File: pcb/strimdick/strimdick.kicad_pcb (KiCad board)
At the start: 2 copper layers, 4 parts, among them U1 ProMicro

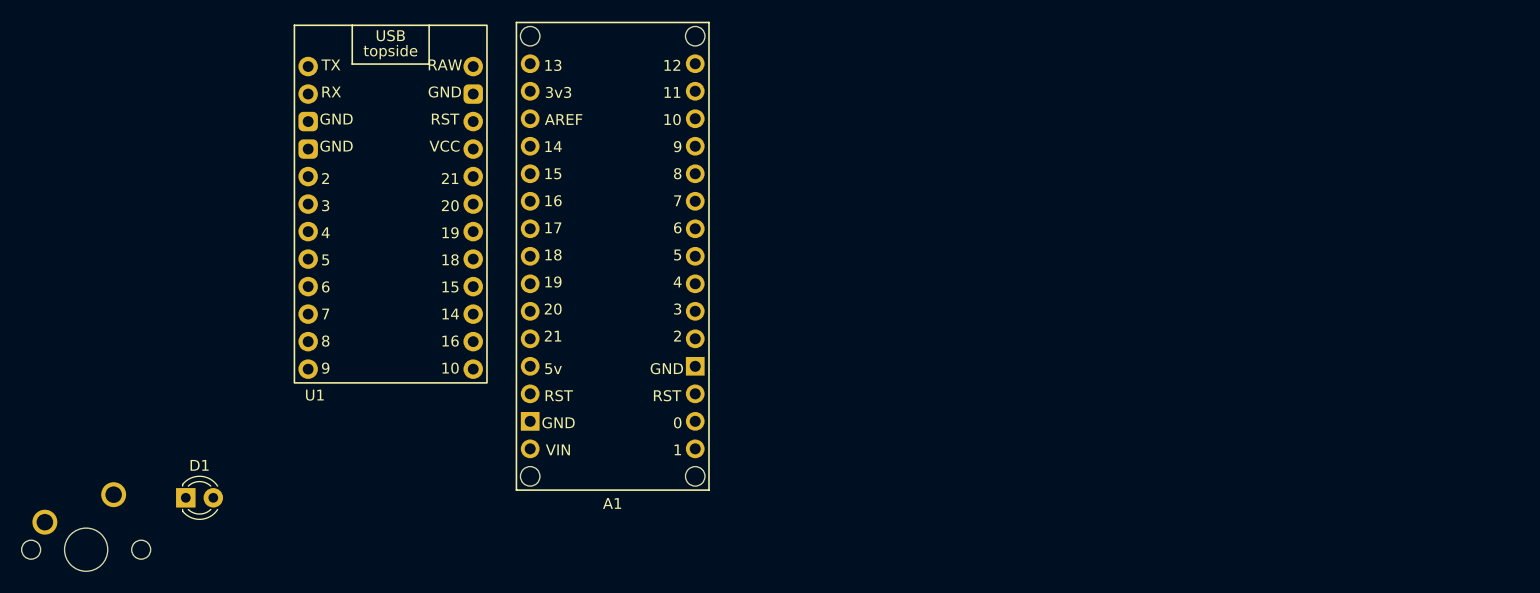
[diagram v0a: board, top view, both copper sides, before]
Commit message: Okay, got the schematic done, and a basic layout with things all stacked up, it's a bit tight
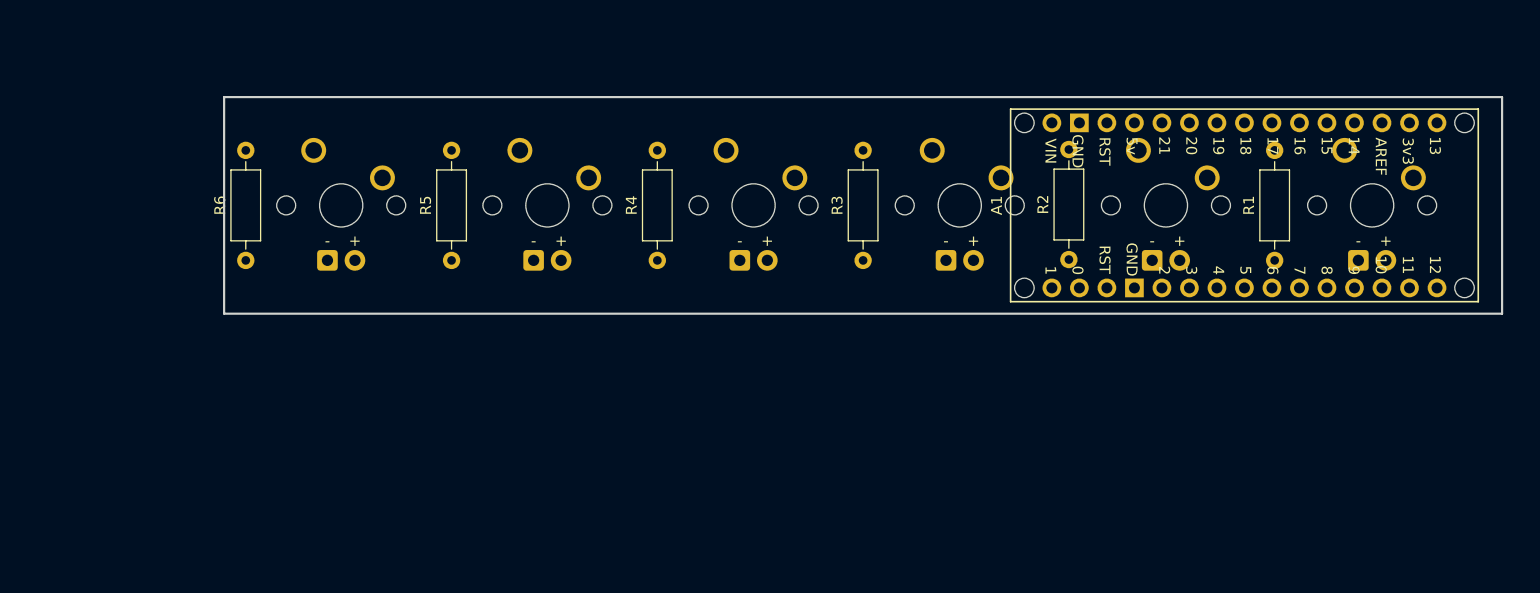
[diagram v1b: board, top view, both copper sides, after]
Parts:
- removed U1: ProMicro, Neko:ProMicro_USBup
- added D2: LED_3mm, PCM_marbastlib-mx:LED_MX_3mm, B.Cu at (156.0, 44.1)
- added D3: LED_3mm, PCM_marbastlib-mx:LED_MX_3mm, B.Cu at (136.9, 44.1)
- added D4: LED_3mm, PCM_marbastlib-mx:LED_MX_3mm, B.Cu at (117.9, 44.1)
- added D5: LED_3mm, PCM_marbastlib-mx:LED_MX_3mm, B.Cu at (98.8, 44.1)
- added D6: LED_3mm, PCM_marbastlib-mx:LED_MX_3mm, B.Cu at (79.8, 44.1)
- added MX2: MX_SW_solder, PCM_marbastlib-mx:SW_MX_1u, B.Cu at (156.0, 39.0)
- added MX3: MX_SW_solder, PCM_marbastlib-mx:SW_MX_1u, B.Cu at (136.9, 39.0)
- added MX4: MX_SW_solder, PCM_marbastlib-mx:SW_MX_1u, B.Cu at (117.9, 39.0)
- added MX5: MX_SW_solder, PCM_marbastlib-mx:SW_MX_1u, B.Cu at (98.8, 39.0)
- added MX6: MX_SW_solder, PCM_marbastlib-mx:SW_MX_1u, B.Cu at (79.8, 39.0)
- added R1: 220ohm, Resistor_THT:R_Axial_DIN0207_L6.3mm_D2.5mm_P10.16mm_Horizontal, F.Cu at (166.0, 44.1)
- added R2: 220ohm, Resistor_THT:R_Axial_DIN0207_L6.3mm_D2.5mm_P10.16mm_Horizontal, F.Cu at (147.0, 44.0)
- added R3: 220ohm, Resistor_THT:R_Axial_DIN0207_L6.3mm_D2.5mm_P10.16mm_Horizontal, F.Cu at (128.0, 44.1)
- added R4: 220ohm, Resistor_THT:R_Axial_DIN0207_L6.3mm_D2.5mm_P10.16mm_Horizontal, F.Cu at (109.0, 44.1)
- added R5: 220ohm, Resistor_THT:R_Axial_DIN0207_L6.3mm_D2.5mm_P10.16mm_Horizontal, F.Cu at (90.0, 44.1)
- added R6: 220ohm, Resistor_THT:R_Axial_DIN0207_L6.3mm_D2.5mm_P10.16mm_Horizontal, F.Cu at (71.0, 44.1)
- D1: footprint LED_THT:LED_D3.0mm -> PCM_marbastlib-mx:LED_MX_3mm; moved to B.Cu
- MX1: moved to B.Cu
- moved MX1 122.9 mm to (175.0, 39.0), turned to 180 degrees
- moved D1 111.7 mm to (175.0, 44.1), turned to 180 degrees
- moved A1 45.5 mm to (142.8, 39.0), turned to -90 degrees
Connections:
- A1 pad 5V: unconnected-(A1-Pad5V) -> Net-(A1-Pad5V)
- A1 pad A2: unconnected-(A1-PadA2) -> Net-(A1-PadA2)
- A1 pad A3: unconnected-(A1-PadA3) -> Net-(A1-PadA3)
- A1 pad A4: unconnected-(A1-A4/SDA-PadA4) -> Net-(A1-A4/SDA)
- A1 pad A5: unconnected-(A1-A5/SCL-PadA5) -> Net-(A1-A5/SCL)
- A1 pad A6: unconnected-(A1-PadA6) -> Net-(A1-PadA6)
- A1 pad A7: unconnected-(A1-PadA7) -> Net-(A1-PadA7)
- A1 pad D11: unconnected-(A1-D11_MOSI-PadD11) -> Net-(A1-D11_MOSI)
- A1 pad D2: unconnected-(A1-D2_INT0-PadD2) -> Net-(A1-D2_INT0)
- A1 pad D3: unconnected-(A1-D3_INT1-PadD3) -> Net-(A1-D3_INT1)
- A1 pad D4: unconnected-(A1-PadD4) -> Net-(A1-PadD4)
- A1 pad D5: unconnected-(A1-PadD5) -> Net-(A1-PadD5)
- A1 pad D6: unconnected-(A1-PadD6) -> Net-(A1-PadD6)
- A1 pad D7: unconnected-(A1-PadD7) -> Net-(A1-PadD7)
- A1 pad D9: unconnected-(A1-PadD9) -> Net-(A1-Pad5V)
- A1 pad GND1: unconnected-(A1-GND-PadGND1) -> Net-(A1-D11_MOSI)
- A1 pad GND2: unconnected-(A1-GND-PadGND2) -> Net-(A1-D11_MOSI)
- D1 pad 1: unconnected-(D1-Pad1) -> Net-(A1-D11_MOSI)
- D1 pad 2: unconnected-(D1-Pad2) -> Net-(D1-Pad2)
- MX1 pad 1: unconnected-(MX1-Pad1) -> Net-(A1-D11_MOSI)
- MX1 pad 2: unconnected-(MX1-Pad2) -> Net-(A1-PadA2)
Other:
- board outline added: 118 x 20 mm

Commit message: Make Design Rules Checker happy
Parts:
- moved R6 0.50 mm to (71.5, 44.1)
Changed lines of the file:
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@@
 	(footprint "Resistor_THT:R_Axial_DIN0207_L6.3mm_D2.5mm_P10.16mm_Horizontal"
 		(layer "F.Cu")
-		(at 71 44.08 90)
+		(at 71.5 44.08 90)
 		(descr "Resistor, Axial_DIN0207 series, Axial, Horizontal, pin pitch=10.16mm, 0.25W = 1/4W, length*diameter=6.3*2.5mm^2, http://cdn-reichelt.de/documents/datenblatt/B400/1_4W%23YAG.pdf")
 		(tags "Resistor Axial_DIN0207 series Axial Horizontal pin pitch 10.16mm 0.25W = 1/4W length 6.3mm diameter 2.5mm")
 		(property "Reference" "R6"
-			(at 5.08 -2.37 90)
+			(at 5.08 0 90)
 			(layer "F.SilkS")
 			(effects
@@
 		(tags "Resistor Axial_DIN0207 series Axial Horizontal pin pitch 10.16mm 0.25W = 1/4W length 6.3mm diameter 2.5mm")
 		(property "Reference" "R2"
-			(at 5.08 -2.37 90)
+			(at 5.08 0 90)
 			(layer "F.SilkS")
 			(effects
@@
 		(tags "Resistor Axial_DIN0207 series Axial Horizontal pin pitch 10.16mm 0.25W = 1/4W length 6.3mm diameter 2.5mm")
 		(property "Reference" "R4"
-			(at 5.08 -2.37 90)
+			(at 5.08 0 90)
 			(layer "F.SilkS")
 			(effects
@@
 		(tags "Resistor Axial_DIN0207 series Axial Horizontal pin pitch 10.16mm 0.25W = 1/4W length 6.3mm diameter 2.5mm")
 		(property "Reference" "R3"
-			(at 5.08 -2.37 90)
+			(at 5.08 0 90)
 			(layer "F.SilkS")
 			(effects
@@
 		(tags "Resistor Axial_DIN0207 series Axial Horizontal pin pitch 10.16mm 0.25W = 1/4W length 6.3mm diameter 2.5mm")
 		(property "Reference" "R1"
-			(at 5.08 -2.37 90)
+			(at 5.08 0 90)
 			(layer "F.SilkS")
 			(effects
@@
 		(tags "Resistor Axial_DIN0207 series Axial Horizontal pin pitch 10.16mm 0.25W = 1/4W length 6.3mm diameter 2.5mm")
 		(property "Reference" "R5"
-			(at 5.08 -2.37 90)
+			(at 5.08 0 90)
 			(layer "F.SilkS")
 			(effects
@@
 		)
 		(fp_line
-			(start 8.89 1.18)
+			(start -4 1.18)
 			(end -8.89 1.18)
 			(stroke
@@
 		(fp_line
 			(start 8.89 1.18)
+			(end 4 1.18)
+			(stroke
+				(width 0.15)
+				(type solid)
+			)
+			(layer "F.SilkS")
+		)
+		(fp_line
+			(start 8.89 1.18)
 			(end 8.89 -42)
 			(stroke
@@
 		)
 		(fp_text user "6"
-			(at 6 -23 -90)
+			(at 6 -22.1995 -90)
 			(unlocked yes)
 			(layer "F.SilkS")
@@
 		)
 		(fp_text user "14"
-			(at -5.5 -30.5 -90)
-			(unlocked yes)
-			(layer "F.SilkS")
-			(effects
-				(font
-					(size 1 1)
-					(thickness 0.15)
-				)
-			)
-		)
-		(fp_text user "9"
-			(at 6 -30.5 -90)
+			(at -5.5 -31.6995 -90)
 			(unlocked yes)
 			(layer "F.SilkS")
@@
 		)
 		(fp_text user "18"
-			(at -5.5 -20.5 -90)
-			(unlocked yes)
-			(layer "F.SilkS")
-			(effects
-				(font
-					(size 1 1)
-					(thickness 0.15)
-				)
-			)
-		)
-		(fp_text user "2"
-			(at 6 -13 -90)
+			(at -5.5 -20.1995 -90)
 			(unlocked yes)
 			(layer "F.SilkS")
@@
 			)
 		)
-		(fp_text user "10"
-			(at 5.5 -33 -90)
-			(unlocked yes)
-			(layer "F.SilkS")
-			(effects
-				(font
-					(size 1 1)
-					(thickness 0.15)
-				)
-			)
-		)
 		(fp_text user "GND"
-			(at -5 -5 -90)
+			(at -5 -5.6995 -90)
 			(unlocked yes)
 			(layer "F.SilkS")
@@
 		)
 		(fp_text user "3"
-			(at 6 -15.5 -90)
+			(at 6 -15.6995 -90)
 			(unlocked yes)
 			(layer "F.SilkS")
@@
 		)
 		(fp_text user "17"
-			(at -5.5 -23 -90)
+			(at -5.5 -21.6995 -90)
 			(unlocked yes)
 			(layer "F.SilkS")
@@
 		)
 		(fp_text user "15"
-			(at -5.5 -28 -90)
+			(at -5.5 -27.1995 -90)
 			(unlocked yes)
 			(layer "F.SilkS")
@@
 		)
 		(fp_text user "5v"
-			(at -5.5 -10 -90)
+			(at -5.5 -8.6995 -90)
 			(unlocked yes)
 			(layer "F.SilkS")
@@
 	)
 	(gr_rect
-		(start 69 29)
-		(end 187 49)
+		(start 69.5 29)
+		(end 187.5 49)
 		(stroke
 			(width 0.2)

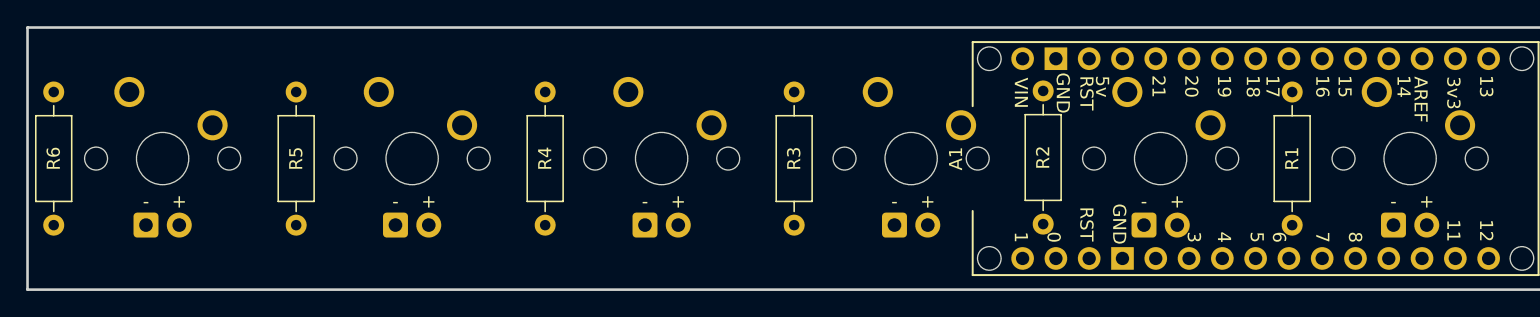
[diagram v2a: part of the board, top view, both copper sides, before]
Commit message: Routing, some silkscreen instructions.
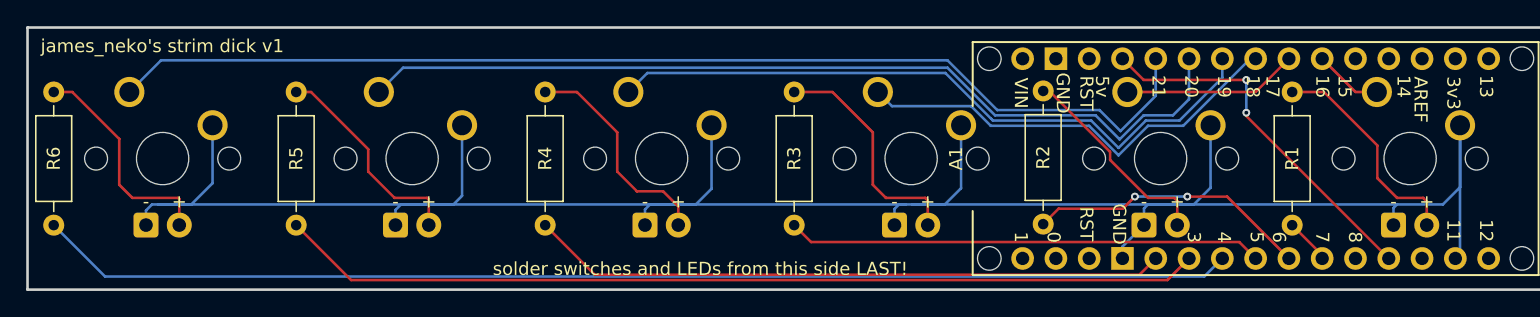
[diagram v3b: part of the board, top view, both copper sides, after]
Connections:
- A1 pad GND2: Net-(A1-D11_MOSI) -> unconnected-(A1-GND-PadGND2)
- R1 pad 1: Net-(A1-D2_INT0) -> Net-(A1-PadD7)
- R2 pad 1: Net-(A1-D3_INT1) -> Net-(A1-PadD6)
- R3 pad 1: Net-(A1-PadD4) -> Net-(A1-PadD5)
- R4 pad 1: Net-(A1-PadD5) -> Net-(A1-D2_INT0)
- R5 pad 1: Net-(A1-PadD6) -> Net-(A1-D3_INT1)
- R6 pad 1: Net-(A1-PadD7) -> Net-(A1-PadD4)
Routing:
- net Net-(A1-D11_MOSI): track 0.00 -> 178.3 mm
- net Net-(A1-PadD4): track 0.00 -> 91.4 mm
- net Net-(A1-PadA7): track 0.00 -> 85.5 mm
- net Net-(A1-D3_INT1): track 0.00 -> 70.5 mm
- net Net-(A1-PadA6): track 0.00 -> 69.2 mm
- net Net-(A1-A5/SCL): track 0.00 -> 52.0 mm
- net Net-(A1-D2_INT0): track 0.00 -> 48.7 mm
- net Net-(A1-PadD5): track 0.00 -> 36.3 mm
- net Net-(A1-A4/SDA): track 0.00 -> 33.9 mm
- net Net-(A1-Pad5V): track 0.00 -> 28.2 mm, vias 0 -> 2
- net Net-(A1-PadD6): track 0.00 -> 21.6 mm, vias 0 -> 2
- net Net-(D3-Pad2): track 0.00 -> 17.8 mm
- net Net-(D6-Pad2): track 0.00 -> 17.0 mm
- net Net-(D1-Pad2): track 0.00 -> 17.0 mm
- net Net-(D4-Pad2): track 0.00 -> 17.0 mm
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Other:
- board text added: "james_neko's strim dick v1"
- board text added: "solder resistors and header pins from this side!"
- board text added: "solder switches and LEDs from this side LAST!"

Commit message: trying this 'add fill' thing
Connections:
- net Net-(A1-D11_MOSI) renamed GND
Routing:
- added copper zone on B.Cu, net GND

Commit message: Add JLC text
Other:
- board text added: "JLCJLCJLCJLC"
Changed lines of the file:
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@@
+		)
+	)
+	(gr_text "JLCJLCJLCJLC"
+		(at 70.5 48 0)
+		(layer "F.SilkS")
+		(effects
+			(font
+				(size 1 1)
+				(thickness 0.1)
+			)
+			(justify left bottom)
 		)
 	)
